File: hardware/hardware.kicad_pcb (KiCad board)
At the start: 2 copper layers, 83 x 54.5 mm, 17 parts, among them J1 Screw_Terminal_01x02, J2 Screw_Terminal_01x02, J3 Screw_Terminal_01x02, K1 RM85-2011-35-1005, K2 RM85-2011-35-1005, Q1 BC337, Q2 BC337, U1 XIAO-ESP32-C6

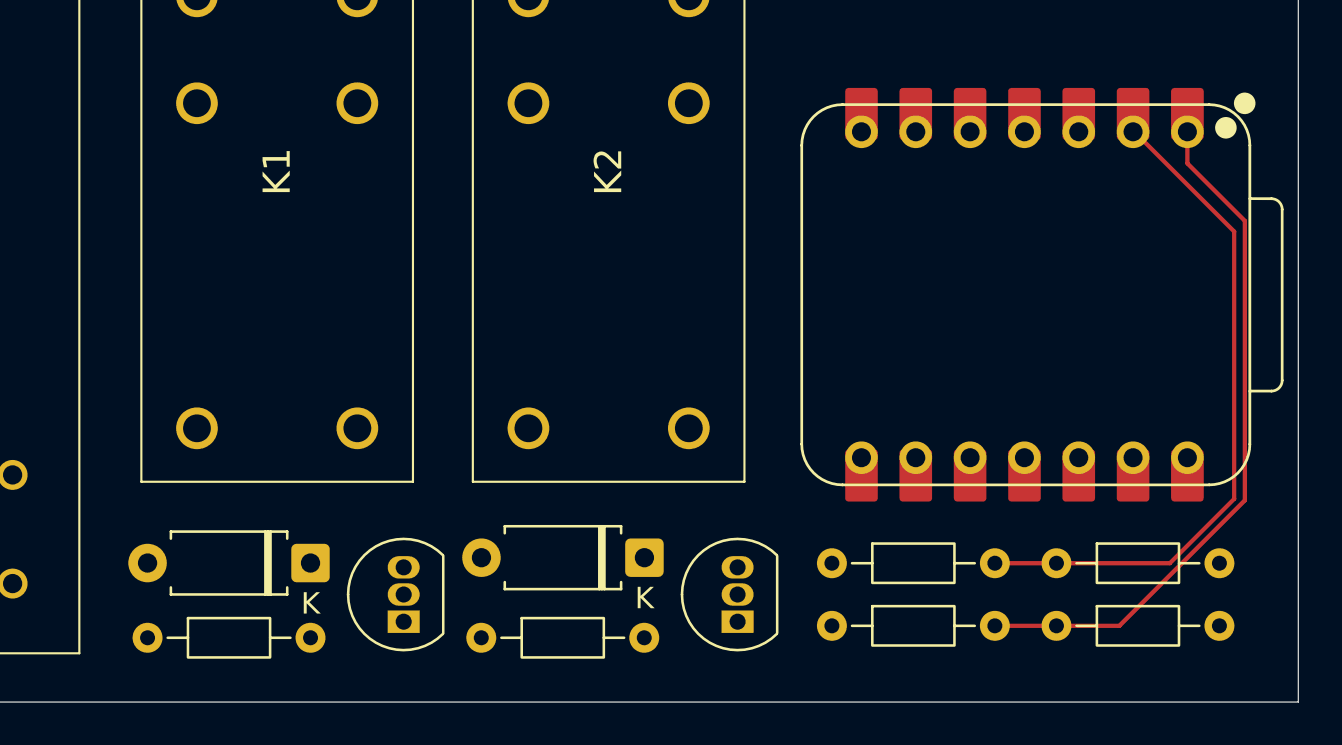
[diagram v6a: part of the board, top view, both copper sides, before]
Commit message: Updated PCB footprint layout
Updatec PCB layout after removing resistors
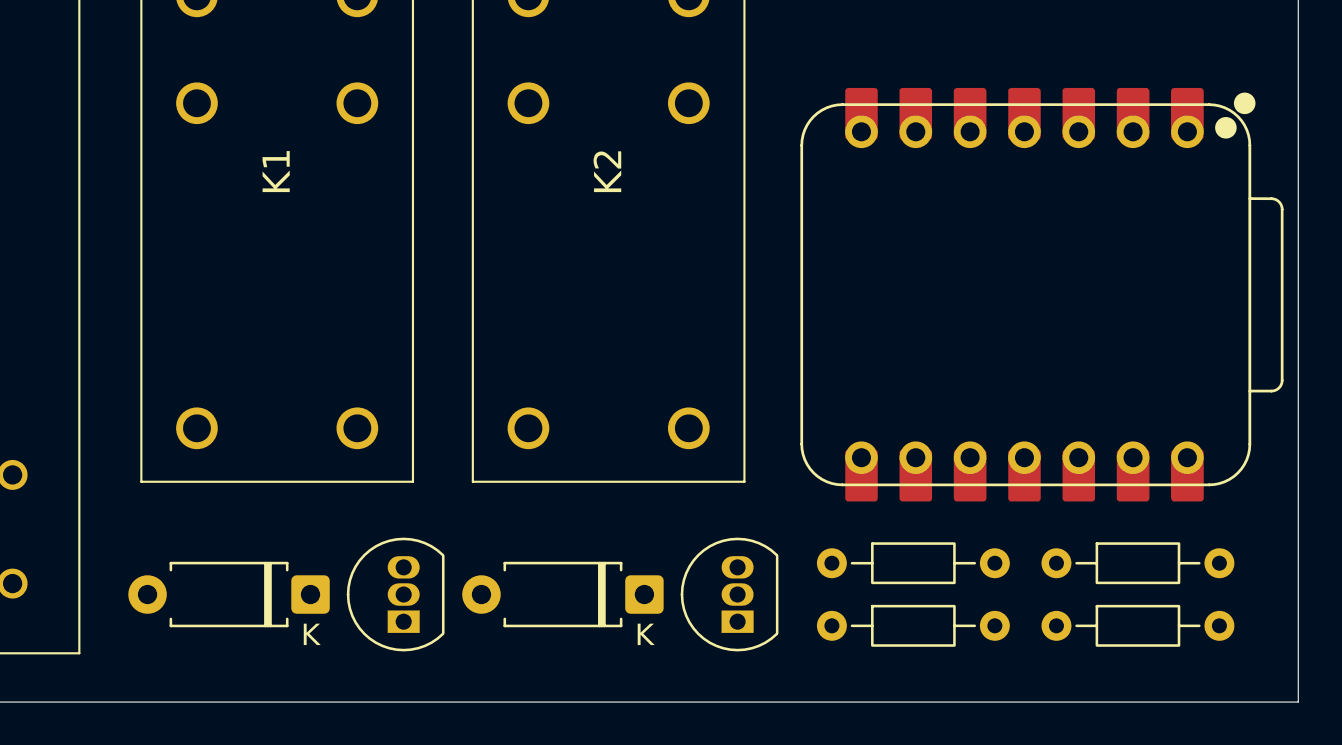
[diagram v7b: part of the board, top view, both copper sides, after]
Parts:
- removed R1, R3: 100R, Resistor_THT:R_Axial_DIN0204_L3.6mm_D1.6mm_P7.62mm_Horizontal
- moved D2 1.72 mm to (67.4, 64.5)
- moved D1 1.47 mm to (51.8, 64.5)
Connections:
- Q1 pad 1: Net-(Q1-C) -> Net-(D1-A)
- Q2 pad 1: Net-(Q2-C) -> Net-(D2-A)
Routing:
- net RELAY_A_CTRL: track 32.5 -> 0.00 mm
- net RELAY_B_CTRL: track 32.4 -> 0.77 mm

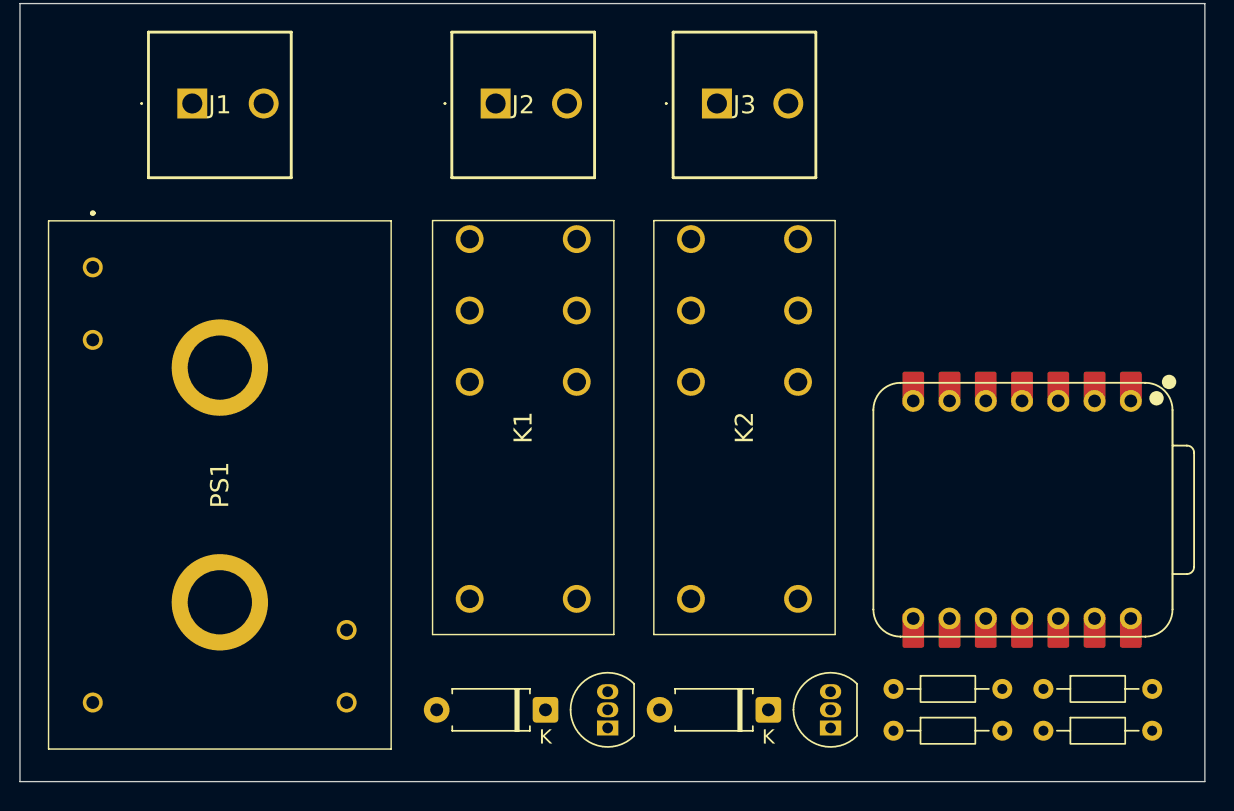
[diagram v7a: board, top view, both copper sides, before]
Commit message: Added PCB traces
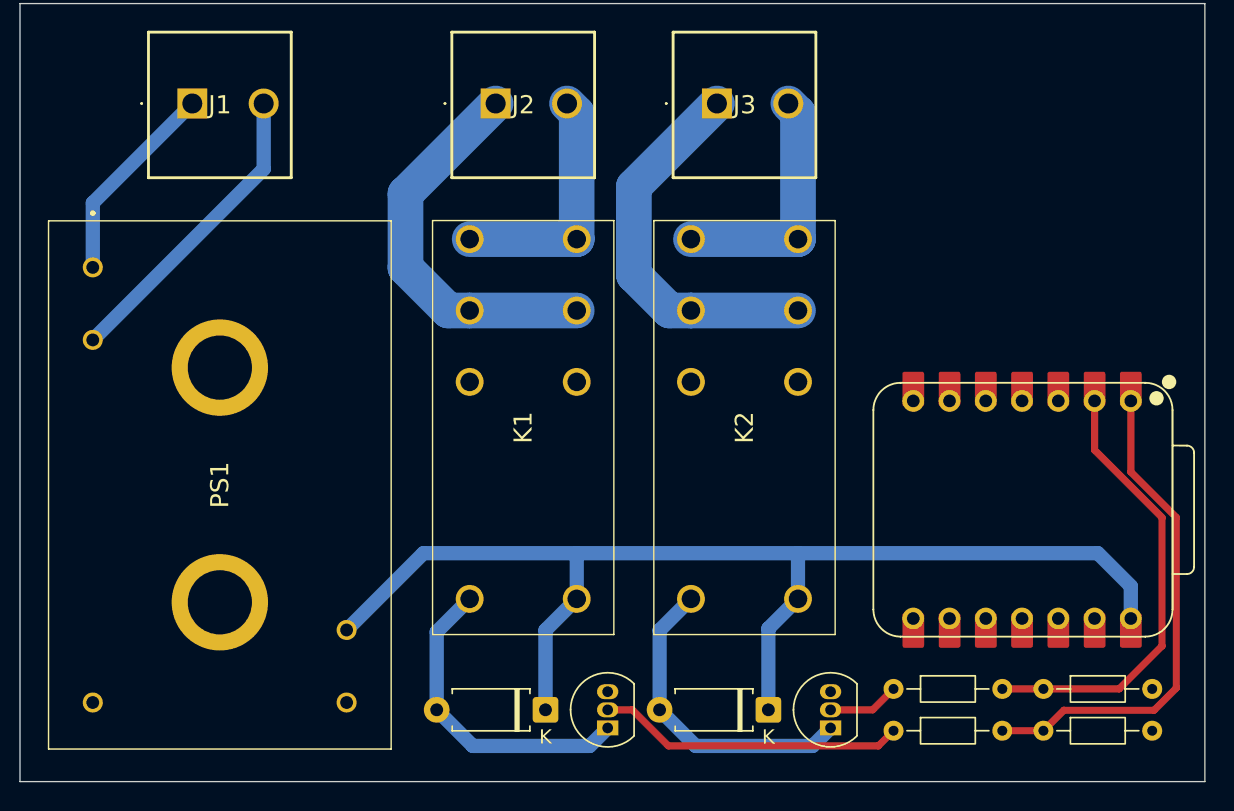
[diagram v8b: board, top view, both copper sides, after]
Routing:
- net +5V: track 0.00 -> 84.1 mm
- net RELAY_A_CTRL: track 0.00 -> 34.9 mm
- net RELAY_B_CTRL: track 0.77 -> 32.3 mm
- net RELAY_A_IN: track 0.00 -> 27.4 mm
- net RELAY_B_IN: track 0.00 -> 26.9 mm
- net Net-(D1-A): track 0.00 -> 22.3 mm
- net Net-(D2-A): track 0.00 -> 22.2 mm
- net 230VAC_N: track 0.00 -> 21.5 mm
- net Net-(Q1-B): track 0.00 -> 21.5 mm
- net RELAY_B_OUT: track 0.00 -> 17.3 mm
- net RELAY_A_OUT: track 0.00 -> 17.3 mm
- net 230VAC_L: track 0.00 -> 14.4 mm
- net Net-(Q2-B): track 0.00 -> 5.02 mm
